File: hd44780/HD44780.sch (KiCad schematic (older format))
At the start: 3 parts

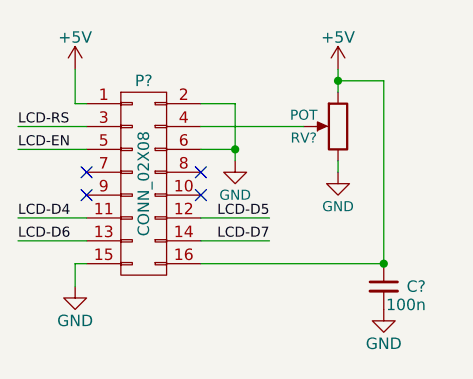
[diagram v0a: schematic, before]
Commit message: Update to KiCad 5
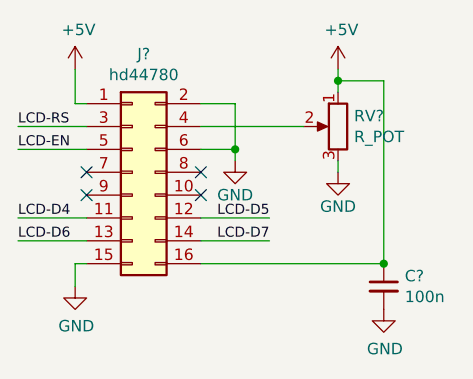
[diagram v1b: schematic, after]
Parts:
- removed C?: 100n, symbol C_Small
- removed P?: CONN_02X08, symbol CONN_02X08
- removed RV?: POT, symbol POT
- added C?: 100n, symbol Device:C_Small
- added J?: hd44780, symbol Connector_Generic:Conn_02x08_Odd_Even
- added RV?: R_POT, symbol Device:R_POT
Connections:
- net +5V: now also C?.1, J?.1 (Pin_1), J?.16 (Pin_16), RV?.1
- net GND: now also C?.2, J?.15 (Pin_15), J?.2 (Pin_2), J?.6 (Pin_6), RV?.3
- net LCD-D4: now also J?.11 (Pin_11)
- net LCD-D5: now also J?.12 (Pin_12)
- net LCD-D6: now also J?.13 (Pin_13)
- net LCD-D7: now also J?.14 (Pin_14)
- net LCD-EN: now also J?.5 (Pin_5)
- net LCD-RS: now also J?.3 (Pin_3)
- new net: J?.4 (Pin_4), RV?.2
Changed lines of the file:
@@
-EESchema Schematic File Version 2
-LIBS:HD44780-rescue
-LIBS:power
-LIBS:device
-LIBS:transistors
-LIBS:conn
-LIBS:linear
-LIBS:regul
-LIBS:74xx
-LIBS:cmos4000
-LIBS:adc-dac
-LIBS:memory
-LIBS:xilinx
-LIBS:microcontrollers
-LIBS:dsp
-LIBS:microchip
-LIBS:analog_switches
-LIBS:motorola
-LIBS:texas
-LIBS:intel
-LIBS:audio
-LIBS:interface
-LIBS:digital-audio
-LIBS:philips
-LIBS:display
-LIBS:cypress
-LIBS:siliconi
-LIBS:opto
-LIBS:atmel
-LIBS:contrib
-LIBS:valves
-LIBS:HD44780-cache
-EELAYER 25 0
+EESchema Schematic File Version 4
+EELAYER 26 0
 EELAYER END
 $Descr A4 11693 8268
 encoding utf-8
 Sheet 1 1
-Title "USB tiny-VT"
-Date "2014-05-11"
-Rev "0.3"
-Comp "LOFITECH"
+Title ""
+Date "2018-08-19"
+Rev ""
+Comp ""
 Comment1 ""
 Comment2 ""
@@
 Comment4 ""
 $EndDescr
-$Comp
-L CONN_02X08 P?
-U 1 1 57432282
-P 9000 2000
-F 0 "P?" H 9000 2450 50  0000 C CNN
-F 1 "CONN_02X08" V 9000 2000 50  0000 C CNN
-F 2 "" H 9000 800 60  0000 C CNN
-F 3 "" H 9000 800 60  0000 C CNN
-	1    9000 2000
-	1    0    0    -1
-$EndComp
 NoConn ~ 9250 1950
 NoConn ~ 9250 2050
 NoConn ~ 8750 2050
 NoConn ~ 8750 1950
-$Comp
-L GND #PWR?
-U 1 1 57432283
-P 8700 2450
-F 0 "#PWR?" H 8700 2200 50  0001 C CNN
-F 1 "GND" H 8700 2300 50  0000 C CNN
-F 2 "" H 8700 2450 60  0000 C CNN
-F 3 "" H 8700 2450 60  0000 C CNN
-	1    8700 2450
-	1    0    0    -1
-$EndComp
-$Comp
-L +5V #PWR?
-U 1 1 57432284
-P 8700 1500
-F 0 "#PWR?" H 8700 1350 50  0001 C CNN
-F 1 "+5V" H 8700 1640 50  0000 C CNN
-F 2 "" H 8700 1500 60  0000 C CNN
-F 3 "" H 8700 1500 60  0000 C CNN
-	1    8700 1500
-	1    0    0    -1
-$EndComp
-$Comp
-L GND #PWR?
-U 1 1 57432285
-P 9400 1900
-F 0 "#PWR?" H 9400 1650 50  0001 C CNN
-F 1 "GND" H 9400 1750 44  0000 C CNN
-F 2 "" H 9400 1900 60  0000 C CNN
-F 3 "" H 9400 1900 60  0000 C CNN
-	1    9400 1900
-	1    0    0    -1
-$EndComp
-$Comp
-L +5V #PWR?
-U 1 1 57432287
-P 9850 1500
-F 0 "#PWR?" H 9850 1350 50  0001 C CNN
-F 1 "+5V" H 9850 1640 50  0000 C CNN
-F 2 "" H 9850 1500 60  0000 C CNN
-F 3 "" H 9850 1500 60  0000 C CNN
-	1    9850 1500
-	1    0    0    -1
-$EndComp
-$Comp
-L GND #PWR?
-U 1 1 57432288
-P 9850 1950
-F 0 "#PWR?" H 9850 1700 50  0001 C CNN
-F 1 "GND" H 9850 1800 44  0000 C CNN
-F 2 "" H 9850 1950 60  0000 C CNN
-F 3 "" H 9850 1950 60  0000 C CNN
-	1    9850 1950
-	1    0    0    -1
-$EndComp
-$Comp
-L C_Small C?
-U 1 1 57432289
-P 10050 2450
-F 0 "C?" H 10150 2450 50  0000 L CNN
-F 1 "100n" H 10060 2370 50  0000 L CNN
-F 2 "" H 10050 2450 60  0000 C CNN
-F 3 "" H 10050 2450 60  0000 C CNN
-	1    10050 2450
-	1    0    0    -1
-$EndComp
-$Comp
-L GND #PWR?
-U 1 1 5743228A
-P 10050 2550
-F 0 "#PWR?" H 10050 2300 50  0001 C CNN
-F 1 "GND" H 10050 2400 50  0000 C CNN
-F 2 "" H 10050 2550 60  0000 C CNN
-F 3 "" H 10050 2550 60  0000 C CNN
-	1    10050 2550
-	1    0    0    -1
-$EndComp
 Wire Wire Line
 	9250 1850 9400 1850
 Wire Wire Line
-	9400 1650 9400 1900
+	9400 1650 9400 1850
 Wire Wire Line
 	9400 1650 9250 1650
@@
 Wire Wire Line
 	9250 2350 10050 2350
-Connection ~ 10050 2350
 Wire Wire Line
 	8750 1650 8700 1650
@@
 Text Label 8450 1750 0    44   ~ 0
 LCD-RS
-Wire Wire Line
-	8450 1750 8750 1750
-Wire Wire Line
-	8450 1850 8750 1850
-Wire Wire Line
-	8450 2150 8750 2150
-Wire Wire Line
-	8450 2250 8750 2250
 Text Label 8450 1850 0    44   ~ 0
 LCD-EN
@@
 Text Label 9550 2250 2    44   ~ 0
 LCD-D7
-$Comp
-L POT RV?
-U 1 1 5982C7EA
-P 9850 1750
-F 0 "RV?" H 10000 1700 44  0000 C CNN
-F 1 "POT" H 10000 1800 44  0000 C CNN
-F 2 "" H 9850 1750 50  0001 C CNN
-F 3 "" H 9850 1750 50  0001 C CNN
-	1    9850 1750
-	-1   0    0    -1
-$EndComp
 Wire Wire Line
 	8700 1650 8700 1500
 Wire Wire Line
-	9850 1600 9850 1500
+	9850 1600 9850 1550
 Wire Wire Line
 	9850 1950 9850 1900
@@
 	10050 1550 9850 1550
 Connection ~ 9850 1550
+Wire Wire Line
+	9400 1850 9400 1900
+Wire Wire Line
+	9850 1550 9850 1500
+$Comp
+L Connector_Generic:Conn_02x08_Odd_Even J?
+U 1 1 5B797694
+P 8950 1950
+F 0 "J?" H 9000 2467 50  0000 C CNN
+F 1 "hd44780" H 9000 2376 50  0000 C CNN
+F 2 "" H 8950 1950 50  0001 C CNN
+F 3 "~" H 8950 1950 50  0001 C CNN
+	1    8950 1950
+	1    0    0    -1
+$EndComp
+Wire Wire Line
+	8450 2250 8750 2250
+Wire Wire Line
+	8450 2150 8750 2150
+Wire Wire Line
+	8450 1850 8750 1850
+Wire Wire Line
+	8450 1750 8750 1750
+$Comp
+L Device:R_POT RV?
+U 1 1 5B798155
+P 9850 1750
+F 0 "RV?" H 9780 1796 50  0000 R CNN
+F 1 "R_POT" H 9780 1705 50  0000 R CNN
+F 2 "" H 9850 1750 50  0001 C CNN
+F 3 "~" H 9850 1750 50  0001 C CNN
+	1    9850 1750
+	-1   0    0    -1
+$EndComp
+$Comp
+L power:GND #PWR?
+U 1 1 5B797680
+P 8700 2450
+F 0 "#PWR?" H 8700 2200 50  0001 C CNN
+F 1 "GND" H 8705 2277 50  0000 C CNN
+F 2 "" H 8700 2450 50  0001 C CNN
+F 3 "" H 8700 2450 50  0001 C CNN
+	1    8700 2450
+	1    0    0    -1
+$EndComp
+$Comp
+L power:GND #PWR?
+U 1 1 5B797698
+P 9400 1900
+F 0 "#PWR?" H 9400 1650 50  0001 C CNN
+F 1 "GND" H 9400 1750 50  0000 C CNN
+F 2 "" H 9400 1900 50  0001 C CNN
+F 3 "" H 9400 1900 50  0001 C CNN
+	1    9400 1900
+	1    0    0    -1
+$EndComp
+$Comp
+L power:GND #PWR?
+U 1 1 5B7976A9
+P 9850 1950
+F 0 "#PWR?" H 9850 1700 50  0001 C CNN
+F 1 "GND" H 9850 1800 50  0000 C CNN
+F 2 "" H 9850 1950 50  0001 C CNN
+F 3 "" H 9850 1950 50  0001 C CNN
+	1    9850 1950
+	1    0    0    -1
+$EndComp
+$Comp
+L Device:C_Small C?
+U 1 1 5B79778C
+P 10050 2450
+F 0 "C?" H 10142 2496 50  0000 L CNN
+F 1 "100n" H 10142 2405 50  0000 L CNN
+F 2 "" H 10050 2450 50  0001 C CNN
+F 3 "~" H 10050 2450 50  0001 C CNN
+	1    10050 2450
+	1    0    0    -1
+$EndComp
+Connection ~ 10050 2350
+$Comp
+L power:GND #PWR?
+U 1 1 5B7977F1
+P 10050 2550
+F 0 "#PWR?" H 10050 2300 50  0001 C CNN
+F 1 "GND" H 10055 2377 50  0000 C CNN
+F 2 "" H 10050 2550 50  0001 C CNN
+F 3 "" H 10050 2550 50  0001 C CNN
+	1    10050 2550
+	1    0    0    -1
+$EndComp
+$Comp
+L power:+5V #PWR?
+U 1 1 5B797836
+P 8700 1500
+F 0 "#PWR?" H 8700 1350 50  0001 C CNN
+F 1 "+5V" H 8715 1673 50  0000 C CNN
+F 2 "" H 8700 1500 50  0001 C CNN
+F 3 "" H 8700 1500 50  0001 C CNN
+	1    8700 1500
+	1    0    0    -1
+$EndComp
+$Comp
+L power:+5V #PWR?
+U 1 1 5B79784E
+P 9850 1500
+F 0 "#PWR?" H 9850 1350 50  0001 C CNN
+F 1 "+5V" H 9865 1673 50  0000 C CNN
+F 2 "" H 9850 1500 50  0001 C CNN
+F 3 "" H 9850 1500 50  0001 C CNN
+	1    9850 1500
+	1    0    0    -1
+$EndComp
 $EndSCHEMATC

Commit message: Pinout for hd44780 was mirrored.
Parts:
- J?: value hd44780 -> HD44780
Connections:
- net +5V: now also J?.15 (Pin_15), J?.2 (Pin_2); no longer J?.1 (Pin_1), J?.16 (Pin_16)
- net GND: now also J?.1 (Pin_1), J?.16 (Pin_16), J?.5 (Pin_5); no longer J?.15 (Pin_15), J?.2 (Pin_2), J?.6 (Pin_6)
- net LCD-EN: now also J?.6 (Pin_6); no longer J?.5 (Pin_5)
- net LCD-RS: now also J?.4 (Pin_4); no longer J?.3 (Pin_3)
- net at RV?.2: now also J?.3 (Pin_3); no longer J?.4 (Pin_4)
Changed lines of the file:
@@
 EESchema Schematic File Version 4
-EELAYER 26 0
+EELAYER 30 0
 EELAYER END
 $Descr A4 11693 8268
@@
 LCD-EN
 Text Label 8450 2150 0    44   ~ 0
-LCD-D4
+LCD-D5
 Text Label 8450 2250 0    44   ~ 0
-LCD-D6
+LCD-D7
 Wire Wire Line
 	9250 2150 9550 2150
@@
 	9250 2250 9550 2250
 Text Label 9550 2150 2    44   ~ 0
-LCD-D5
+LCD-D4
 Text Label 9550 2250 2    44   ~ 0
-LCD-D7
+LCD-D6
 Wire Wire Line
 	8700 1650 8700 1500
@@
 L Connector_Generic:Conn_02x08_Odd_Even J?
 U 1 1 5B797694
-P 8950 1950
-F 0 "J?" H 9000 2467 50  0000 C CNN
-F 1 "hd44780" H 9000 2376 50  0000 C CNN
-F 2 "" H 8950 1950 50  0001 C CNN
-F 3 "~" H 8950 1950 50  0001 C CNN
-	1    8950 1950
-	1    0    0    -1
+P 9050 1950
+F 0 "J?" H 9100 2467 50  0000 C CNN
+F 1 "HD44780" H 9100 2376 50  0000 C CNN
+F 2 "" H 9050 1950 50  0001 C CNN
+F 3 "~" H 9050 1950 50  0001 C CNN
+	1    9050 1950
+	-1   0    0    -1
 $EndComp
 Wire Wire Line
